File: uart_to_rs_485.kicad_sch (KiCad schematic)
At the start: 19 parts, among them U5 SN65HVD1782DR

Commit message: Updated library name, updated and verified all footprints
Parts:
- C16: symbol EASYEDA2KICAD:C_47u_X5R_0805 -> LiveAstra:C_47u_X5R_0805; now in the parts list
- C17, C18: symbol EASYEDA2KICAD:C_100nF_X7R_0402 -> LiveAstra:C_100nF_X7R_0402
- R14, R15: symbol EASYEDA2KICAD:R_0Ohm_0805_125mW -> LiveAstra:R_0Ohm_0805_125mW
- R16, R17, R18: symbol EASYEDA2KICAD:R_10kOhm_0402_62mW -> LiveAstra:R_10kOhm_0402_62mW
- R19, R20: symbol EASYEDA2KICAD:R_10Ohm_0402_62mW -> LiveAstra:R_10Ohm_0402_62mW
- TP23, TP24, TP25, TP26, TP27, TP28, TP29, TP30: symbol EASYEDA2KICAD:TestPoint_Thimble -> LiveAstra:TestPoint_Thimble
- U5: footprint EASYEDA2KICAD:SOIC-8-R-PDSO-G8 -> LiveAstra:RS_485_SN65HVD1782DR; symbol EASYEDA2KICAD:U_SN65HVD1782DR_RS485_Transiver_Fault_Protected_SOIC8 -> LiveAstra:U_SN65HVD1782DR_RS485_Transiver_Fault_Protected_SOIC8
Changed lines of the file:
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@@
 	)
 	(symbol
-		(lib_id "EASYEDA2KICAD:TestPoint_Thimble")
+		(lib_id "LiveAstra:TestPoint_Thimble")
 		(at 127 134.62 0)
 		(unit 1)
@@
 	)
 	(symbol
-		(lib_id "EASYEDA2KICAD:TestPoint_Thimble")
+		(lib_id "LiveAstra:TestPoint_Thimble")
 		(at 127 88.9 0)
 		(unit 1)
@@
 	)
 	(symbol
-		(lib_id "EASYEDA2KICAD:C_47u_X5R_0805")
+		(lib_id "LiveAstra:C_47u_X5R_0805")
 		(at 71.12 55.88 90)
 		(unit 1)
 		(exclude_from_sim no)
-		(in_bom no)
+		(in_bom yes)
 		(on_board yes)
 		(dnp yes)
@@
 	)
 	(symbol
-		(lib_id "EASYEDA2KICAD:TestPoint_Thimble")
+		(lib_id "LiveAstra:TestPoint_Thimble")
 		(at 195.58 88.9 0)
 		(unit 1)
@@
 	)
 	(symbol
-		(lib_id "EASYEDA2KICAD:TestPoint_Thimble")
+		(lib_id "LiveAstra:TestPoint_Thimble")
 		(at 127 99.06 0)
 		(unit 1)
@@
 	)
 	(symbol
-		(lib_id "EASYEDA2KICAD:R_10Ohm_0402_62mW")
+		(lib_id "LiveAstra:R_10Ohm_0402_62mW")
 		(at 177.8 91.44 0)
 		(unit 1)
@@
 	)
 	(symbol
-		(lib_id "EASYEDA2KICAD:TestPoint_Thimble")
+		(lib_id "LiveAstra:TestPoint_Thimble")
 		(at 195.58 109.22 0)
 		(unit 1)
@@
 	)
 	(symbol
-		(lib_id "EASYEDA2KICAD:R_0Ohm_0805_125mW")
+		(lib_id "LiveAstra:R_0Ohm_0805_125mW")
 		(at 91.44 91.44 0)
 		(unit 1)
@@
 	)
 	(symbol
-		(lib_id "EASYEDA2KICAD:C_100nF_X7R_0402")
+		(lib_id "LiveAstra:C_100nF_X7R_0402")
 		(at 92.71 54.61 90)
 		(unit 1)
@@
 	)
 	(symbol
-		(lib_id "EASYEDA2KICAD:R_10kOhm_0402_62mW")
+		(lib_id "LiveAstra:R_10kOhm_0402_62mW")
 		(at 106.68 144.78 90)
 		(unit 1)
@@
 	)
 	(symbol
-		(lib_id "EASYEDA2KICAD:TestPoint_Thimble")
+		(lib_id "LiveAstra:TestPoint_Thimble")
 		(at 127 45.72 0)
 		(unit 1)
@@
 	)
 	(symbol
-		(lib_id "EASYEDA2KICAD:U_SN65HVD1782DR_RS485_Transiver_Fault_Protected_SOIC8")
+		(lib_id "LiveAstra:U_SN65HVD1782DR_RS485_Transiver_Fault_Protected_SOIC8")
 		(at 152.4 101.6 0)
 		(unit 1)
@@
 			)
 		)
-		(property "Footprint" "EASYEDA2KICAD:SOIC-8-R-PDSO-G8"
+		(property "Footprint" "LiveAstra:RS_485_SN65HVD1782DR"
 			(at 152.4 148.59 0)
 			(effects
@@
 	)
 	(symbol
-		(lib_id "EASYEDA2KICAD:R_10Ohm_0402_62mW")
+		(lib_id "LiveAstra:R_10Ohm_0402_62mW")
 		(at 177.8 111.76 0)
 		(unit 1)
@@
 	)
 	(symbol
-		(lib_id "EASYEDA2KICAD:C_100nF_X7R_0402")
+		(lib_id "LiveAstra:C_100nF_X7R_0402")
 		(at 113.03 54.61 90)
 		(unit 1)
@@
 	)
 	(symbol
-		(lib_id "EASYEDA2KICAD:R_10kOhm_0402_62mW")
+		(lib_id "LiveAstra:R_10kOhm_0402_62mW")
 		(at 106.68 83.82 90)
 		(unit 1)
@@
 	)
 	(symbol
-		(lib_id "EASYEDA2KICAD:R_0Ohm_0805_125mW")
+		(lib_id "LiveAstra:R_0Ohm_0805_125mW")
 		(at 63.5 101.6 0)
 		(unit 1)
@@
 	)
 	(symbol
-		(lib_id "EASYEDA2KICAD:TestPoint_Thimble")
+		(lib_id "LiveAstra:TestPoint_Thimble")
 		(at 170.18 132.08 0)
 		(unit 1)
@@
 	)
 	(symbol
-		(lib_id "EASYEDA2KICAD:R_10kOhm_0402_62mW")
+		(lib_id "LiveAstra:R_10kOhm_0402_62mW")
 		(at 106.68 119.38 90)
 		(unit 1)
@@
 	)
 	(symbol
-		(lib_id "EASYEDA2KICAD:TestPoint_Thimble")
+		(lib_id "LiveAstra:TestPoint_Thimble")
 		(at 127 109.22 0)
 		(unit 1)

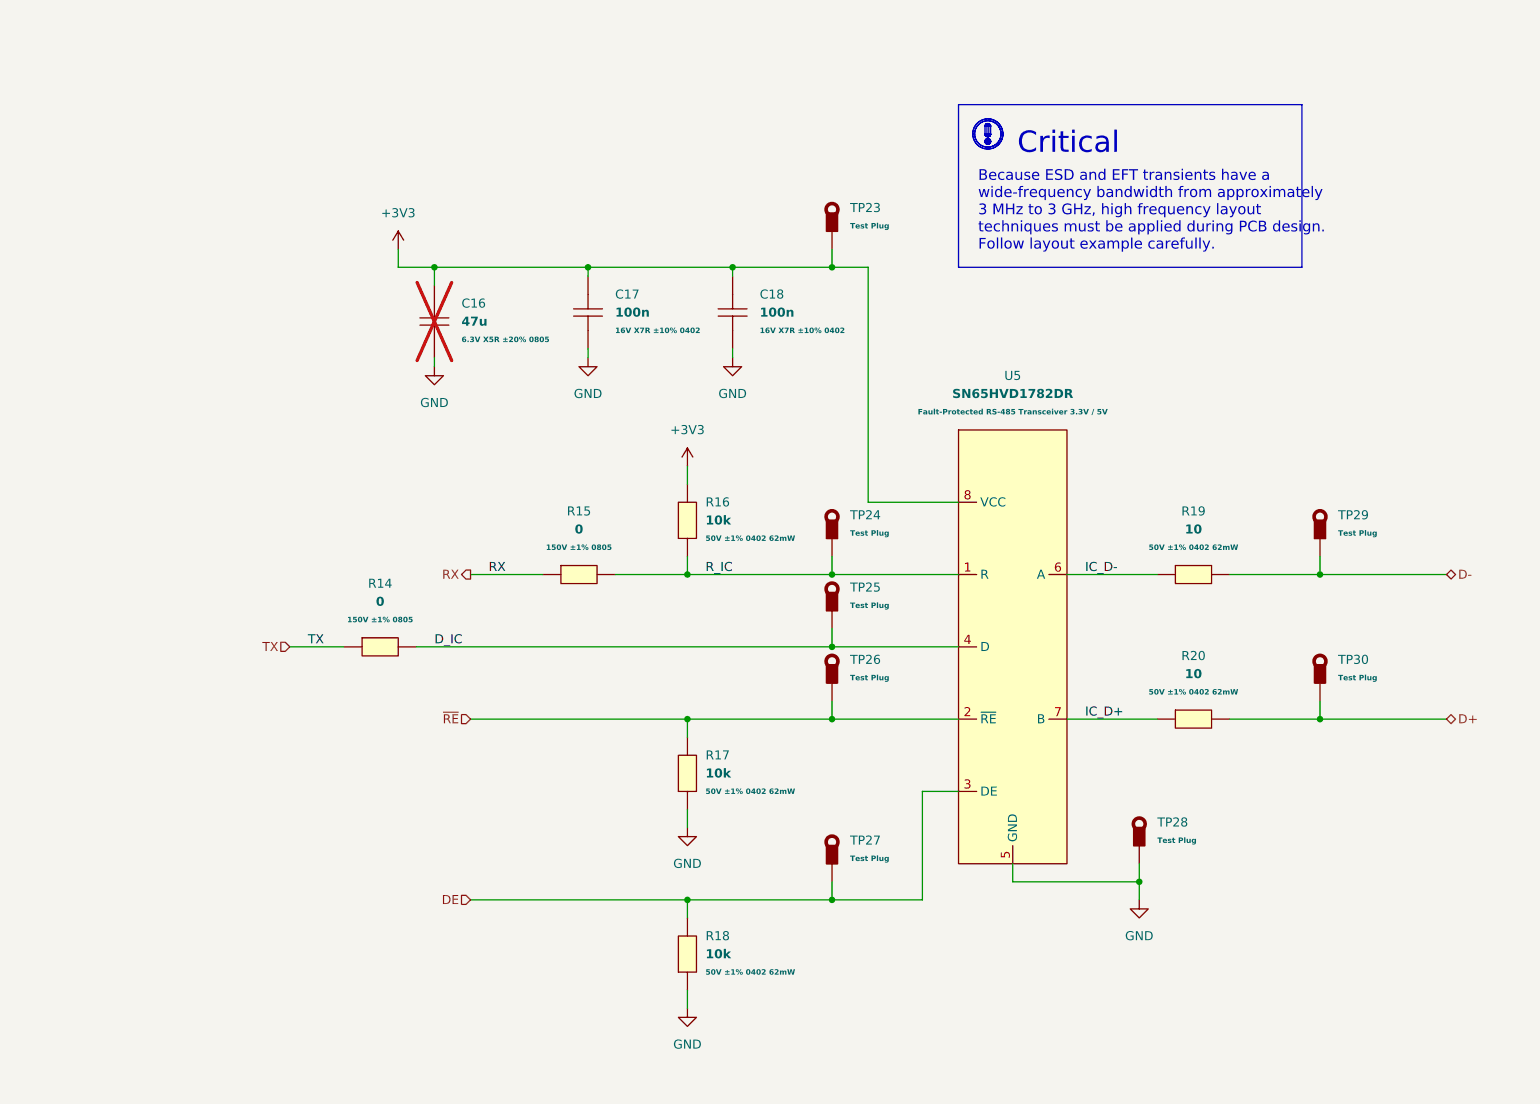
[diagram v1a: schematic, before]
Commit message: Finished layout no drc or erc errors
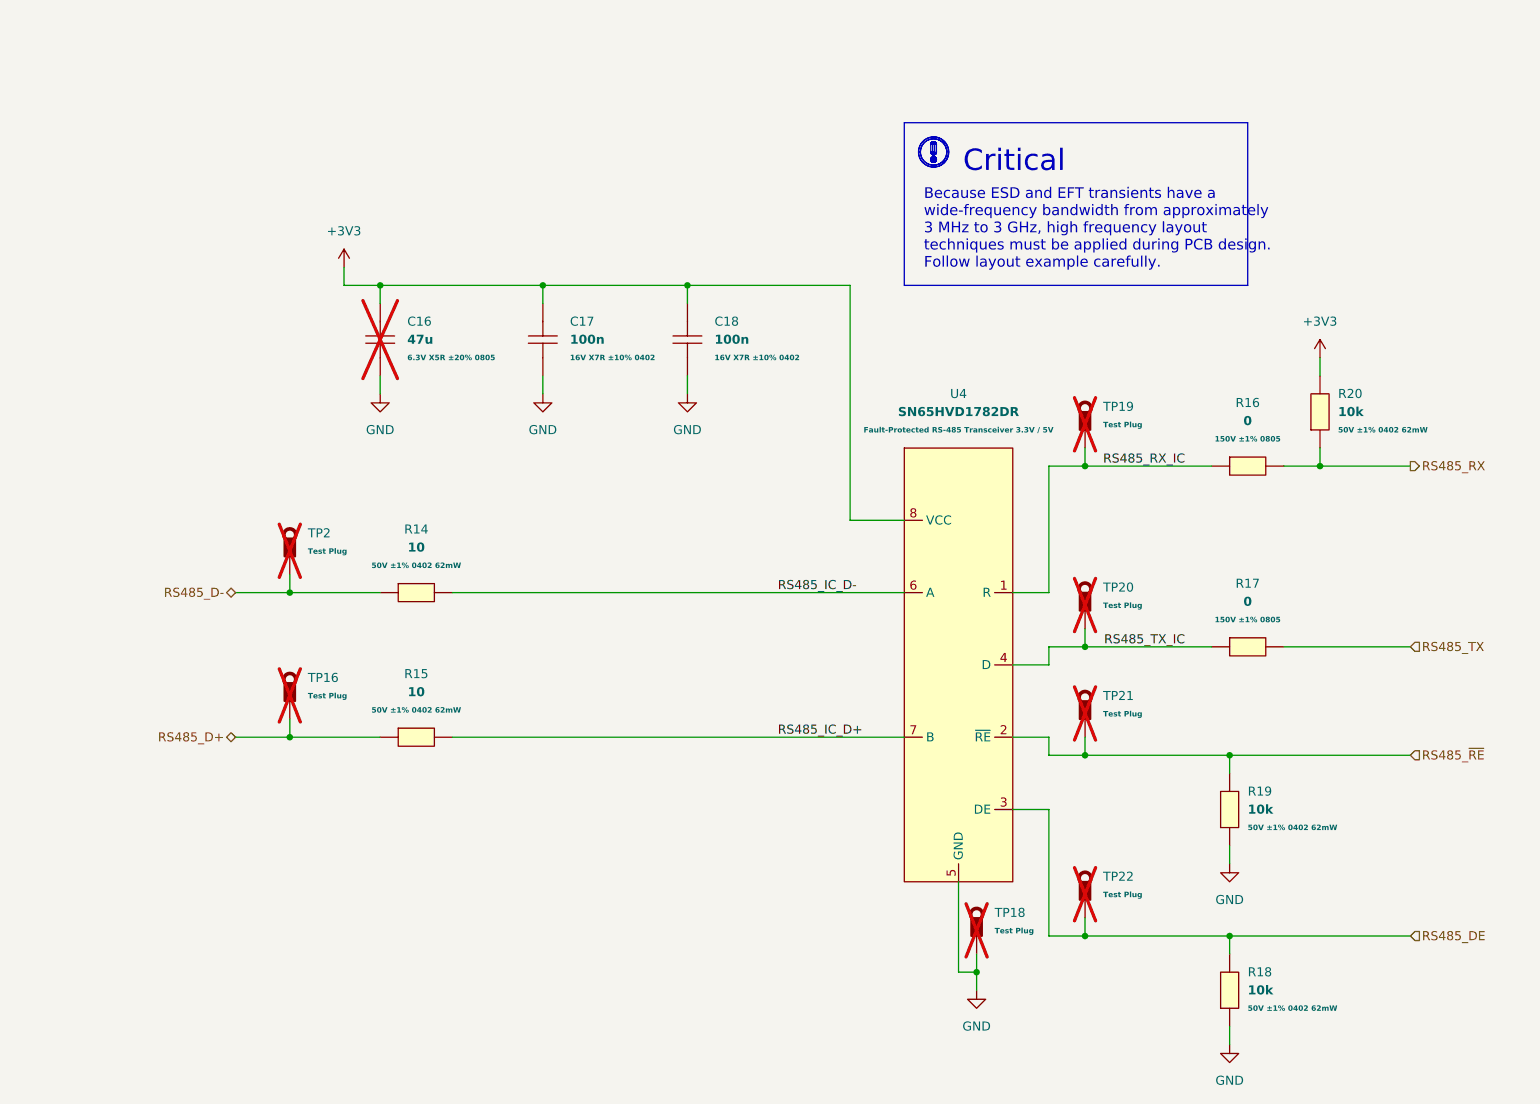
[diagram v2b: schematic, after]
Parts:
- removed R14, R15: 0, Resistor_SMD:R_0805_2012Metric_Pad1.20x1.40mm_HandSolder, symbol LiveAstra:R_0Ohm_0805_125mW
- removed R16, R17: 10k, Resistor_SMD:R_0402_1005Metric, symbol LiveAstra:R_10kOhm_0402_62mW
- removed R19, R20: 10, Resistor_SMD:R_0402_1005Metric, symbol LiveAstra:R_10Ohm_0402_62mW
- removed TP23, TP24, TP25, TP26, TP27, TP28, TP29, TP30: TestPoint_Thimble, TestPoint:TestPoint_Loop_D3.50mm_Drill0.9mm_Beaded, symbol LiveAstra:TestPoint_Thimble
- removed U5: SN65HVD1782DR, LiveAstra:RS_485_SN65HVD1782DR, symbol LiveAstra:U_SN65HVD1782DR_RS485_Transiver_Fault_Protected_SOIC8
- added R14, R15: 10, LiveAstra:R_0402_1005Metric, symbol LiveAstra:R_10Ohm_0402_62mW
- added R16, R17: 0, LiveAstra:R_0805_2012Metric_Pad1.20x1.40mm_HandSolder, symbol LiveAstra:R_0Ohm_0805_125mW
- added R19, R20: 10k, LiveAstra:R_0402_1005Metric, symbol LiveAstra:R_10kOhm_0402_62mW
- added TP16, TP18, TP19, TP2, TP20, TP21, TP22: TestPoint_Thimble, LiveAstra:TestPoint_Loop_D3.50mm_Drill0.9mm_Beaded, symbol LiveAstra:TestPoint_Thimble
- added U4: SN65HVD1782DR, LiveAstra:RS_485_SN65HVD1782DR, symbol LiveAstra:U_SN65HVD1782DR_RS485_Transiver_Fault_Protected_SOIC8
- C16: footprint Capacitor_SMD:C_0805_2012Metric_Pad1.18x1.45mm_HandSolder -> LiveAstra:C_0805_2012Metric_Pad1.18x1.45mm_HandSolder
- C17, C18: footprint Capacitor_SMD:C_0402_1005Metric -> LiveAstra:C_0402_1005Metric
- R18: footprint Resistor_SMD:R_0402_1005Metric -> LiveAstra:R_0402_1005Metric
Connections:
- net +3V3: now also R20.2, U4.8 (VCC)
- net GND: now also R19.1, TP18.1, U4.5 (GND)
- net DE renamed RS485_DE
- net RS485_DE: now also TP22.1, U4.3 (DE)
- new net RS485_D+: R15.1, TP16.1
- new net RS485_D-: R14.1, TP2.1
- new net RS485_IC_D+: R15.2, U4.7 (B)
- new net RS485_IC_D-: R14.2, U4.6 (A)
- new net RS485_RX: R16.2, R20.1
- new net RS485_RX_IC: R16.1, TP19.1, U4.1 (R)
- new net RS485_TX: R17.2
- new net RS485_TX_IC: R17.1, TP20.1, U4.4 (D)
- new net RS485_~{RE}: R19.2, TP21.1, U4.2 (~{RE})

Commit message: Work on kibot
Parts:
- C16: Extra Values 6.3V X5R ±20% 0805 -> 6.3V X5R ±20% 0805

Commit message: workflow
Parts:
- TP16, TP18, TP19, TP2, TP20, TP21, TP22: now fitted
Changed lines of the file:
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@@
+			)
+		)
+		(property "Extra Value" ""
+			(at 68.58 93.98 0)
+			(effects
+				(font
+					(size 1.27 1.27)
+				)
+				(hide yes)
 			)
 		)
@@
 			)
 		)
+		(property "Extra Value" ""
+			(at 195.58 68.58 0)
+			(effects
+				(font
+					(size 1.27 1.27)
+				)
+				(hide yes)
+			)
+		)
 		(pin "1"
 		)
@@
 			)
 		)
+		(property "Extra Value" ""
+			(at 68.58 114.3 0)
+			(effects
+				(font
+					(size 1.27 1.27)
+				)
+				(hide yes)
+			)
+		)
 		(pin "1"
 		)
@@
 			)
 		)
+		(property "Extra Value" ""
+			(at 185.42 101.6 0)
+			(effects
+				(font
+					(size 1.27 1.27)
+				)
+				(hide yes)
+			)
+		)
 		(pin "1"
 		)
@@
 		(in_bom no)
 		(on_board yes)
-		(dnp yes)
+		(dnp no)
 		(fields_autoplaced yes)
 		(property "Reference" "TP18"
@@
 			)
 		)
+		(property "Extra Value" ""
+			(at 147.32 144.78 0)
+			(effects
+				(font
+					(size 1.27 1.27)
+				)
+				(hide yes)
+			)
+		)
 		(pin "1"
 		)
@@
 		(in_bom no)
 		(on_board yes)
-		(dnp yes)
+		(dnp no)
 		(fields_autoplaced yes)
 		(property "Reference" "TP16"
@@
 			)
 		)
+		(property "Extra Value" ""
+			(at 50.8 111.76 0)
+			(effects
+				(font
+					(size 1.27 1.27)
+				)
+				(hide yes)
+			)
+		)
 		(pin "1"
 		)
@@
 			)
 		)
+		(property "Extra Value" ""
+			(at 182.88 149.86 0)
+			(effects
+				(font
+					(size 1.27 1.27)
+				)
+				(hide yes)
+			)
+		)
 		(pin "1"
 		)
@@
 			)
 		)
+		(property "Extra Value" ""
+			(at 182.88 124.46 0)
+			(effects
+				(font
+					(size 1.27 1.27)
+				)
+				(hide yes)
+			)
+		)
 		(pin "1"
 		)
@@
 		(in_bom no)
 		(on_board yes)
-		(dnp yes)
+		(dnp no)
 		(fields_autoplaced yes)
 		(property "Reference" "TP21"
@@
 			)
 		)
+		(property "Extra Value" ""
+			(at 162.56 114.3 0)
+			(effects
+				(font
+					(size 1.27 1.27)
+				)
+				(hide yes)
+			)
+		)
 		(pin "1"
 		)
@@
 			)
 		)
+		(property "Extra Value" ""
+			(at 106.68 58.42 0)
+			(effects
+				(font
+					(size 1.27 1.27)
+				)
+				(hide yes)
+			)
+		)
 		(pin "1"
 		)
@@
 			)
 		)
+		(property "Extra Value" ""
+			(at 144.78 104.14 0)
+			(effects
+				(font
+					(size 1.27 1.27)
+				)
+				(hide yes)
+			)
+		)
 		(pin "3"
 		)
@@
 			)
 		)
+		(property "Extra Value" ""
+			(at 185.42 76.2 0)
+			(effects
+				(font
+					(size 1.27 1.27)
+				)
+				(hide yes)
+			)
+		)
 		(pin "1"
 		)
@@
 		(in_bom no)
 		(on_board yes)
-		(dnp yes)
+		(dnp no)
 		(fields_autoplaced yes)
 		(property "Reference" "TP2"
@@
 			)
 		)
+		(property "Extra Value" ""
+			(at 50.8 91.44 0)
+			(effects
+				(font
+					(size 1.27 1.27)
+				)
+				(hide yes)
+			)
+		)
 		(pin "1"
 		)
@@
 			)
 		)
+		(property "Extra Value" ""
+			(at 63.5 58.42 0)
+			(effects
+				(font
+					(size 1.27 1.27)
+				)
+				(hide yes)
+			)
+		)
 		(pin "1"
 		)
@@
 		(in_bom no)
 		(on_board yes)
-		(dnp yes)
+		(dnp no)
 		(fields_autoplaced yes)
 		(property "Reference" "TP19"
@@
 			)
 		)
+		(property "Extra Value" ""
+			(at 162.56 73.66 0)
+			(effects
+				(font
+					(size 1.27 1.27)
+				)
+				(hide yes)
+			)
+		)
 		(pin "1"
 		)
@@
 		(in_bom no)
 		(on_board yes)
-		(dnp yes)
+		(dnp no)
 		(fields_autoplaced yes)
 		(property "Reference" "TP20"
@@
 			)
 		)
+		(property "Extra Value" ""
+			(at 162.56 99.06 0)
+			(effects
+				(font
+					(size 1.27 1.27)
+				)
+				(hide yes)
+			)
+		)
 		(pin "1"
 		)
@@
 		(in_bom no)
 		(on_board yes)
-		(dnp yes)
+		(dnp no)
 		(fields_autoplaced yes)
 		(property "Reference" "TP22"
@@
 			)
 		)
+		(property "Extra Value" ""
+			(at 162.56 139.7 0)
+			(effects
+				(font
+					(size 1.27 1.27)
+				)
+				(hide yes)
+			)
+		)
 		(pin "1"
 		)
@@
 			)
 		)
+		(property "Extra Value" ""
+			(at 86.36 58.42 0)
+			(effects
+				(font
+					(size 1.27 1.27)
+				)
+				(hide yes)
+			)
+		)

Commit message: workflow
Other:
- title: (none) -> UART to RS-485
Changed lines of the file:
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@@
 	(generator_version "8.0")
 	(paper "A4")
+	(title_block
+		(title "UART to RS-485")
+	)
 	(junction
 		(at 182.88 116.84)
@@
 		)
 		(stroke
+			(width 0)
+			(type default)
+		)
+	)
+	(polyline
+		(pts
+			(xy 12.0708 12.6956) (xy 12.0748 12.6996)
+		)
+		(stroke
